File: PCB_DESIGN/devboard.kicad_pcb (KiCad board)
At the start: 2 copper layers, 21 x 51 mm, 33 parts, among them J1 USB_C_Receptacle_USB2.0_14P, J2 Conn_01x20, J3 Conn_01x20, J4 Conn_01x03, SW1 SW_Push, U1 RP2040, U2 MCP1700x-330xxTT, U4 W25Q16JVUXIQ TR, Y1 12 MHz

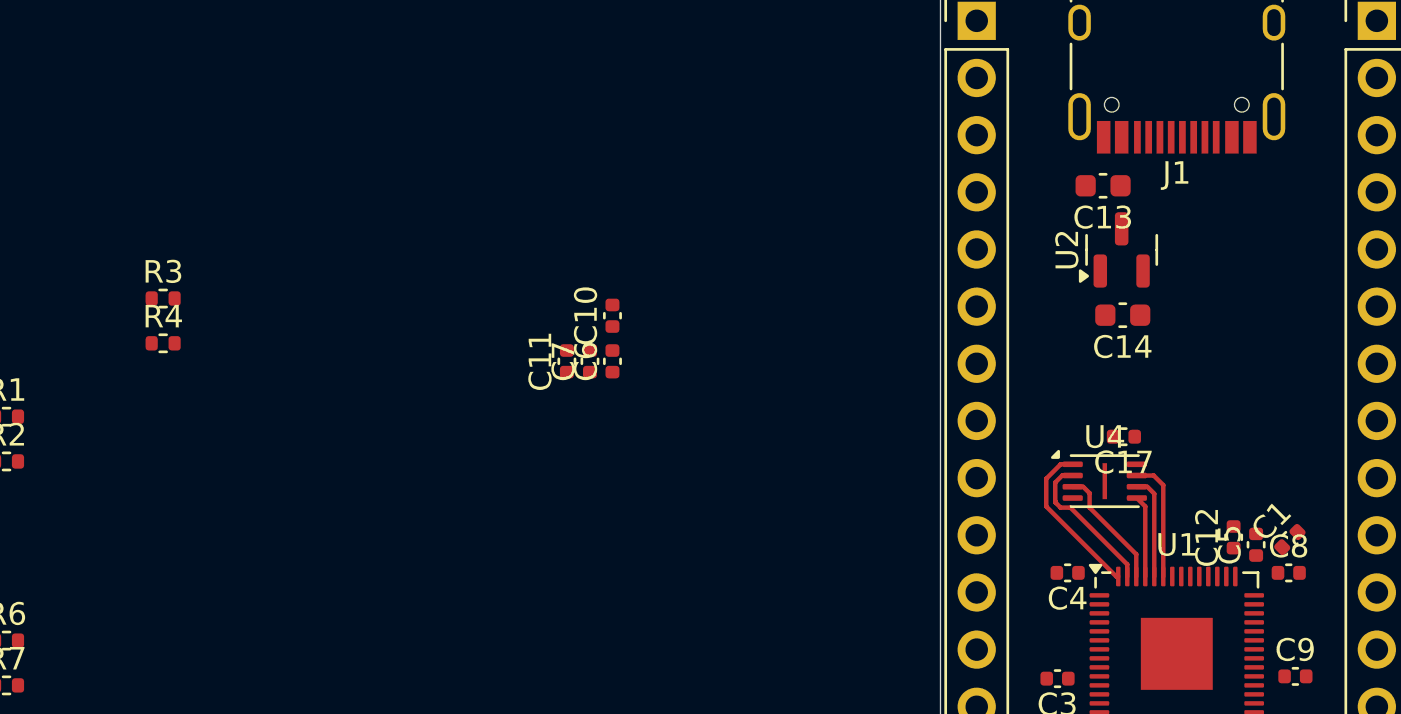
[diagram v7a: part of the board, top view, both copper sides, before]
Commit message: routing differential pairs
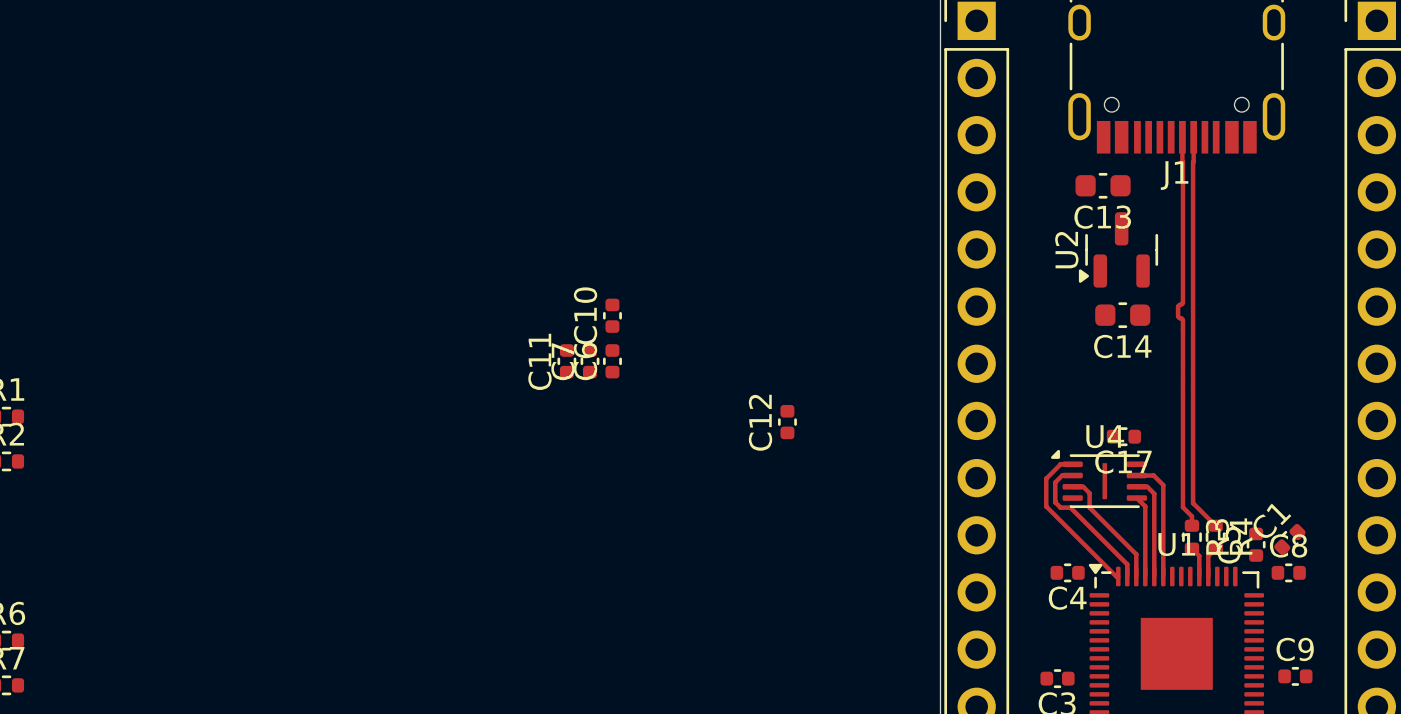
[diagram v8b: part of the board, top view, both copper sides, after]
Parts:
- moved R4 47.6 mm to (162.4, 71.1), turned to -90 degrees
- moved R3 46.9 mm to (161.3, 71.1), turned to -90 degrees
- moved C12 20.5 mm to (143.3, 66.0)
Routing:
- net /USB_DN: track 0.00 -> 17.7 mm
- net /USB_DP: track 0.00 -> 17.7 mm
- net Net-(U1-USB_DP): track 0.00 -> 1.37 mm
- net Net-(U1-USB_DM): track 0.00 -> 1.37 mm
